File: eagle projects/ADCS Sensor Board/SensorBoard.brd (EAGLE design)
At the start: 91 x 91 mm, 113 parts, among them J1 HDR_10_EZFET_DEBUGGER, J3 HDR_2X5_GRPB052VWQS-RC, Q1 PMV16XN, Q2 IRLML6246TRPBF, Q3 IRLML2246TRPBF, U1 MSP430F5529IPN, U2 LMV321, U3 ADS7841E_2K5, U4 LMV321, U5 LMV321, U7 HMC1053, Y1 32.768kHz, Y2 CSTCR4M00G15L99, Y3 32.768kHz

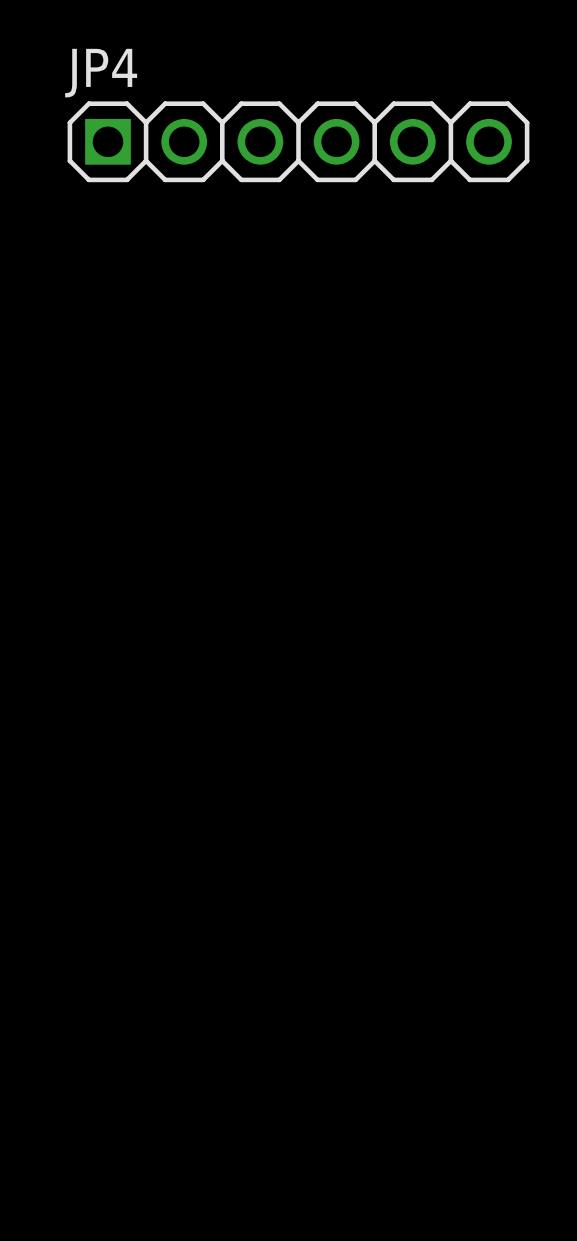
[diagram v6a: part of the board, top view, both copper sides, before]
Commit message: tied floating pins on sensor board
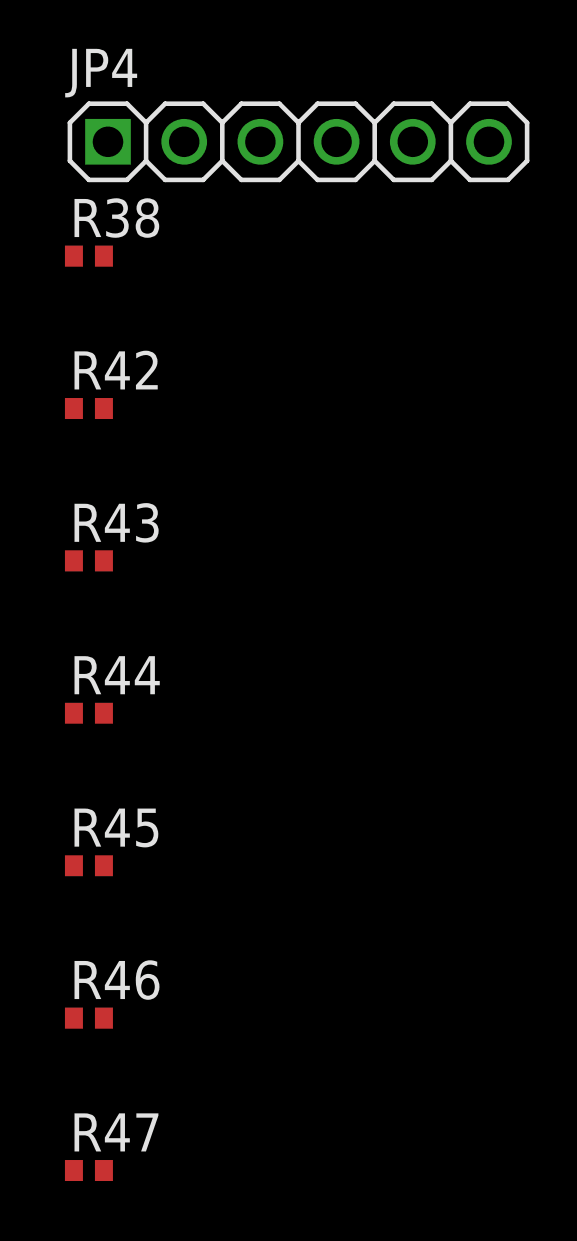
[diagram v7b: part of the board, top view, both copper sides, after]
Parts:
- added R38, R42, R43, R44, R45, R46, R47: 5.1M, rcl:R0402
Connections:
- new net N$30: R38.2, U3.13
- new net N$32: J1.2, R42.1
- new net N$33: J1.10, R43.1
- new net N$34: R46.1, U1.67
- new net N$38: R47.1, U1.66
- net GND: now also R38.1, R42.2, R43.2, R44.2, R45.2, R46.2, R47.2
- net N$18: now also R45.1
- net N$19: now also R44.1
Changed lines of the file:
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@@
 </layers>
 <board>
-<fusionsync huburn="a.YnVzaW5lc3M6bXlkYWwyMA" projecturn="a.YnVzaW5lc3M6bXlkYWwyMCMyMDIxMDExNjM3MjQwMzc3Ng" f3durn="urn:adsk.wipprod:dm.lineage:oVI3oCs-TfOfufbVRd14pQ" pcbguid="" lastpulledtime="" lastsyncedchangeguid="" latestrevisionid="538ff946-eeda-4d0e-ad1a-fac0754e7cb5" lastsyncedrevisionid="538ff946-eeda-4d0e-ad1a-fac0754e7cb5" lastboardhashguid="366b6101-3844-e8b1-004e-a3535860192e" lastpushedtime="2021-02-27T16:58:43Z" linktopcb3d="true"/>
+<fusionsync huburn="a.YnVzaW5lc3M6bXlkYWwyMA" projecturn="a.YnVzaW5lc3M6bXlkYWwyMCMyMDIxMDExNjM3MjQwMzc3Ng" f3durn="urn:adsk.wipprod:dm.lineage:oVI3oCs-TfOfufbVRd14pQ" pcbguid="" lastpulledtime="" lastsyncedchangeguid="" latestrevisionid="538ff946-eeda-4d0e-ad1a-fac0754e7cb5" lastsyncedrevisionid="538ff946-eeda-4d0e-ad1a-fac0754e7cb5" lastboardhashguid="366b6101-3844-e8b1-004e-a3535860192e" lastpushedtime="2021-02-27T16:58:43Z" linktopcb3d="false"/>
 <plain>
 <wire x1="0" y1="0" x2="31.5" y2="0" width="0.1524" layer="20"/>
@@
 <attribute name="POPULARITY" value="79" x="3.81" y="-22.86" size="1.778" layer="27" display="off"/>
 </element>
+<element name="R38" library="rcl" library_urn="urn:adsk.eagle:library:334" package="R0402" package3d_urn="urn:adsk.eagle:package:23547/3" value="5.1M" x="-3.175" y="-26.67" smashed="yes">
+<attribute name="NAME" x="-3.81" y="-26.035" size="1.27" layer="25"/>
+<attribute name="POPULARITY" value="34" x="-3.175" y="-26.67" size="1.778" layer="27" display="off"/>
+<attribute name="SPICEPREFIX" value="R" x="-3.175" y="-26.67" size="1.778" layer="27" display="off"/>
+<attribute name="VALUE" x="-3.81" y="-28.575" size="1.27" layer="27"/>
+</element>
+<element name="R42" library="rcl" library_urn="urn:adsk.eagle:library:334" package="R0402" package3d_urn="urn:adsk.eagle:package:23547/3" value="5.1M" x="-3.175" y="-31.75" smashed="yes">
+<attribute name="NAME" x="-3.81" y="-31.115" size="1.27" layer="25"/>
+<attribute name="POPULARITY" value="34" x="-3.175" y="-31.75" size="1.778" layer="27" display="off"/>
+<attribute name="SPICEPREFIX" value="R" x="-3.175" y="-31.75" size="1.778" layer="27" display="off"/>
+<attribute name="VALUE" x="-3.81" y="-33.655" size="1.27" layer="27"/>
+</element>
+<element name="R43" library="rcl" library_urn="urn:adsk.eagle:library:334" package="R0402" package3d_urn="urn:adsk.eagle:package:23547/3" value="5.1M" x="-3.175" y="-36.83" smashed="yes">
+<attribute name="NAME" x="-3.81" y="-36.195" size="1.27" layer="25"/>
+<attribute name="POPULARITY" value="34" x="-3.175" y="-36.83" size="1.778" layer="27" display="off"/>
+<attribute name="SPICEPREFIX" value="R" x="-3.175" y="-36.83" size="1.778" layer="27" display="off"/>
+<attribute name="VALUE" x="-3.81" y="-38.735" size="1.27" layer="27"/>
+</element>
+<element name="R44" library="rcl" library_urn="urn:adsk.eagle:library:334" package="R0402" package3d_urn="urn:adsk.eagle:package:23547/3" value="5.1M" x="-3.175" y="-41.91" smashed="yes">
+<attribute name="NAME" x="-3.81" y="-41.275" size="1.27" layer="25"/>
+<attribute name="POPULARITY" value="34" x="-3.175" y="-41.91" size="1.778" layer="27" display="off"/>
+<attribute name="SPICEPREFIX" value="R" x="-3.175" y="-41.91" size="1.778" layer="27" display="off"/>
+<attribute name="VALUE" x="-3.81" y="-43.815" size="1.27" layer="27"/>
+</element>
+<element name="R45" library="rcl" library_urn="urn:adsk.eagle:library:334" package="R0402" package3d_urn="urn:adsk.eagle:package:23547/3" value="5.1M" x="-3.175" y="-46.99" smashed="yes">
+<attribute name="NAME" x="-3.81" y="-46.355" size="1.27" layer="25"/>
+<attribute name="POPULARITY" value="34" x="-3.175" y="-46.99" size="1.778" layer="27" display="off"/>
+<attribute name="SPICEPREFIX" value="R" x="-3.175" y="-46.99" size="1.778" layer="27" display="off"/>
+<attribute name="VALUE" x="-3.81" y="-48.895" size="1.27" layer="27"/>
+</element>
+<element name="R46" library="rcl" library_urn="urn:adsk.eagle:library:334" package="R0402" package3d_urn="urn:adsk.eagle:package:23547/3" value="5.1M" x="-3.175" y="-52.07" smashed="yes">
+<attribute name="NAME" x="-3.81" y="-51.435" size="1.27" layer="25"/>
+<attribute name="POPULARITY" value="34" x="-3.175" y="-52.07" size="1.778" layer="27" display="off"/>
+<attribute name="SPICEPREFIX" value="R" x="-3.175" y="-52.07" size="1.778" layer="27" display="off"/>
+<attribute name="VALUE" x="-3.81" y="-53.975" size="1.27" layer="27"/>
+</element>
+<element name="R47" library="rcl" library_urn="urn:adsk.eagle:library:334" package="R0402" package3d_urn="urn:adsk.eagle:package:23547/3" value="5.1M" x="-3.175" y="-57.15" smashed="yes">
+<attribute name="NAME" x="-3.81" y="-56.515" size="1.27" layer="25"/>
+<attribute name="POPULARITY" value="34" x="-3.175" y="-57.15" size="1.778" layer="27" display="off"/>
+<attribute name="SPICEPREFIX" value="R" x="-3.175" y="-57.15" size="1.778" layer="27" display="off"/>
+<attribute name="VALUE" x="-3.81" y="-59.055" size="1.27" layer="27"/>
+</element>
 </elements>
 <signals>
@@
 <contactref element="C29" pad="2"/>
 <contactref element="JP4" pad="6"/>
+<contactref element="R38" pad="1"/>
+<contactref element="R42" pad="2"/>
+<contactref element="R43" pad="2"/>
+<contactref element="R44" pad="2"/>
+<contactref element="R45" pad="2"/>
+<contactref element="R46" pad="2"/>
+<contactref element="R47" pad="2"/>
 <wire x1="73.025" y1="87.1056" x2="78.4225" y2="86.995" width="0" layer="19" extent="1-1"/>
 <wire x1="68.8975" y1="86.995" x2="73.025" y2="87.1056" width="0" layer="19" extent="1-1"/>
@@
 <wire x1="13.97" y1="86.6775" x2="28.2575" y2="86.6775" width="0" layer="19" extent="1-1"/>
 <wire x1="-1.69" y1="-10.16" x2="10.4775" y2="2.8575" width="0" layer="19" extent="1-1"/>
-<wire x1="10.16" y1="-22.86" x2="-1.69" y2="-10.16" width="0" layer="19" extent="1-1"/>
+<wire x1="-3.675" y1="-26.67" x2="-1.69" y2="-10.16" width="0" layer="19" extent="1-1"/>
+<wire x1="-2.675" y1="-31.75" x2="-3.675" y2="-26.67" width="0" layer="19" extent="1-1"/>
+<wire x1="-2.675" y1="-36.83" x2="-2.675" y2="-31.75" width="0" layer="19" extent="1-1"/>
+<wire x1="-2.675" y1="-41.91" x2="-2.675" y2="-36.83" width="0" layer="19" extent="1-1"/>
+<wire x1="-2.675" y1="-46.99" x2="-2.675" y2="-41.91" width="0" layer="19" extent="1-1"/>
+<wire x1="-2.675" y1="-52.07" x2="-2.675" y2="-46.99" width="0" layer="19" extent="1-1"/>
+<wire x1="-2.675" y1="-57.15" x2="-2.675" y2="-52.07" width="0" layer="19" extent="1-1"/>
+<wire x1="10.16" y1="-22.86" x2="-3.675" y2="-26.67" width="0" layer="19" extent="1-1"/>
 </signal>
 <signal name="TARGET_PUR">
@@
 <signal name="N$18">
 <contactref element="JP2" pad="8"/>
-</signal>
-<signal name="N$19">
-<contactref element="JP2" pad="10"/>
+<contactref element="R45" pad="1"/>
+<wire x1="-3.675" y1="-46.99" x2="67.31" y2="12.7" width="0" layer="19" extent="1-1"/>
 </signal>
 <signal name="!CS!_SUN_Y+">
@@
 <contactref element="JP4" pad="5"/>
 </signal>
+<signal name="N$30">
+<contactref element="U3" pad="13"/>
+<contactref element="R38" pad="2"/>
+<wire x1="-2.675" y1="-26.67" x2="48.5902" y2="45.4025" width="0" layer="19" extent="1-1"/>
+</signal>
+<signal name="N$32">
+<contactref element="J1" pad="2"/>
+<contactref element="R42" pad="1"/>
+<wire x1="-3.675" y1="-31.75" x2="88.265" y2="36.195" width="0" layer="19" extent="1-1"/>
+</signal>
+<signal name="N$33">
+<contactref element="J1" pad="10"/>
+<contactref element="R43" pad="1"/>
+<wire x1="-3.675" y1="-36.83" x2="88.265" y2="15.875" width="0" layer="19" extent="1-1"/>
+</signal>
+<signal name="N$19">
+<contactref element="JP2" pad="10"/>
+<contactref element="R44" pad="1"/>
+<wire x1="-3.675" y1="-41.91" x2="69.85" y2="12.7" width="0" layer="19" extent="1-1"/>
+</signal>
+<signal name="N$34">
+<contactref element="U1" pad="67"/>
+<contactref element="R46" pad="1"/>
+<wire x1="-3.675" y1="-52.07" x2="74.575" y2="42.7" width="0" layer="19" extent="1-1"/>
+</signal>
+<signal name="N$38">
+<contactref element="U1" pad="66"/>
+<contactref element="R47" pad="1"/>
+<wire x1="-3.675" y1="-57.15" x2="74.575" y2="42.2" width="0" layer="19" extent="1-1"/>
+</signal>
 </signals>
